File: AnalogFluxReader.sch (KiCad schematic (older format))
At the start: 54 parts, among them J1 , J2 , J3 , J4 , U1 AD9235BR, U2 74HC393, U3 AD8138, U4 74HC06, U5 74HC06, U6 LM2664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

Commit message: Updated schematic. Use 74AC163 and 74AC153 instead.
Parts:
- removed D1, D2, D3, D4, D5: BAT54HMFH, symbol Device:D
- removed JP1, JP2, JP3, JP4, JP5, JP6, JP7, JP8: Jumper, symbol Device:Jumper
- removed R3: 1k, symbol Device:R
- removed U2: 74HC393, symbol 74xx:74LS393
- removed unit 2 of U4
- removed unit 1 of U5
- added U2: 74AC163, symbol 74xx:74LS163
- added U8: 74AC153, symbol 74xx:74LS153
- C10, C11: value 100n -> 15p
- C12, C9: value CP_Small -> 47u
- R10, R9: value 1k -> 22
- U4: value 74HC06 -> 74HC14
- U5: value 74HC06 -> 74HC05
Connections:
- net labels added: CLKSEL0, CLKSEL1
- net labels removed: DSKCHG, REDWC
- wire segments 254 -> 255
- no-connect marks 13 -> 17

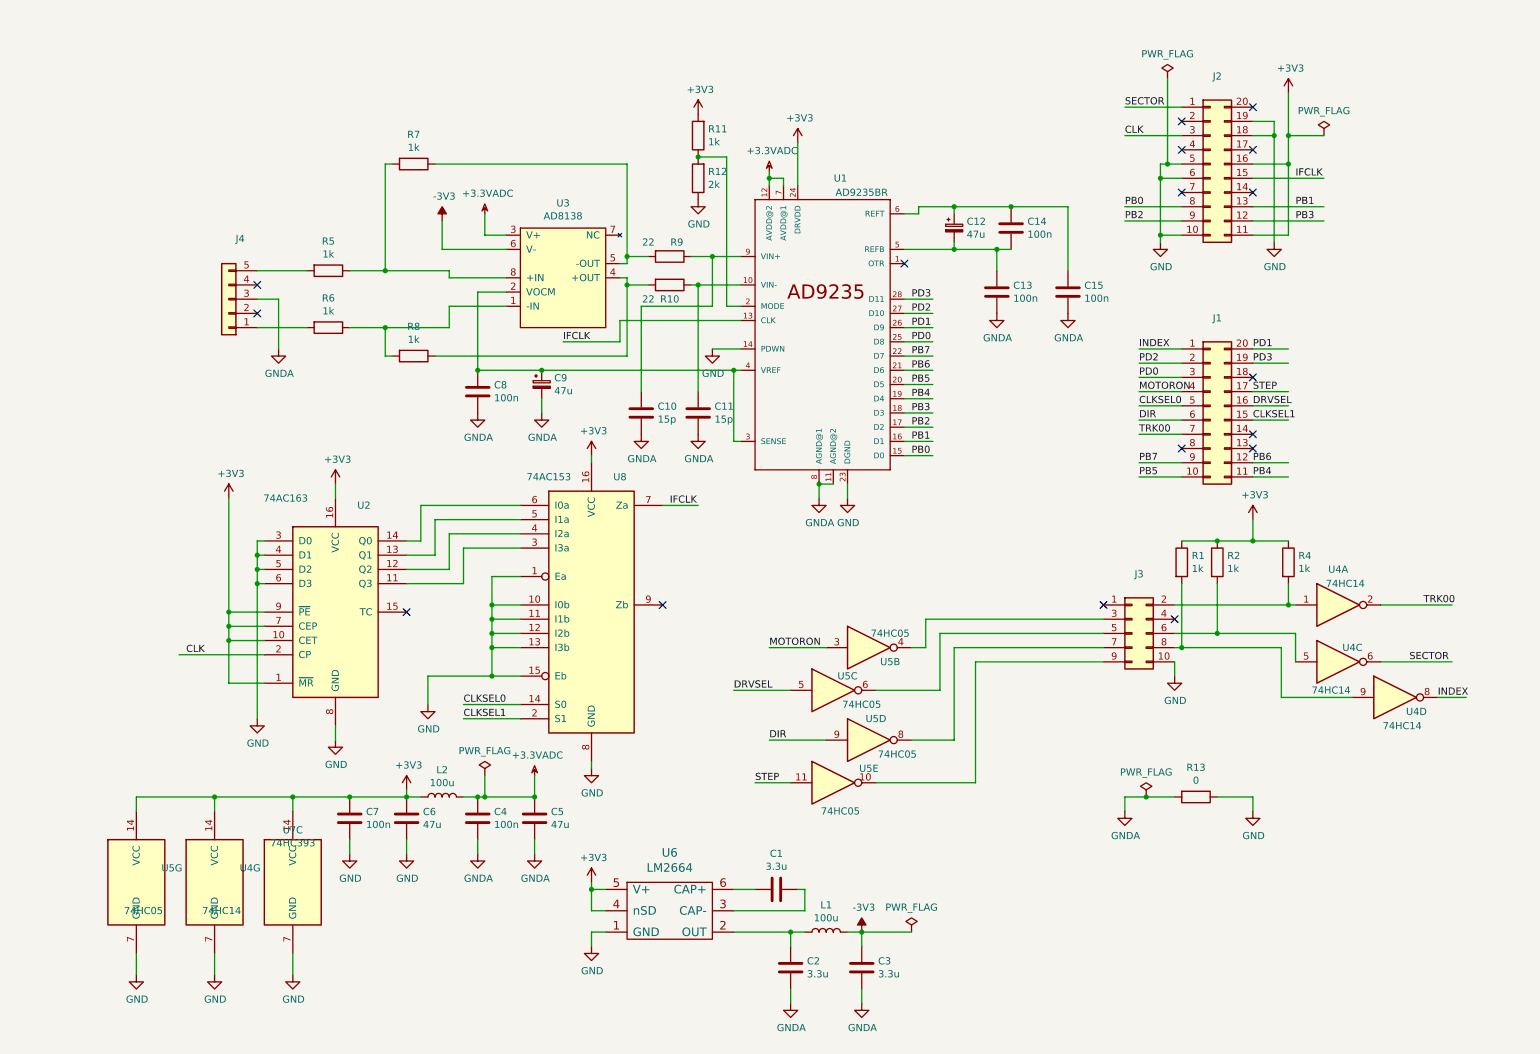
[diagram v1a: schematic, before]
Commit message: Introduced MCP23017 to handle low speed floppy signals. Several PAx pins needed for Slave FIFO.
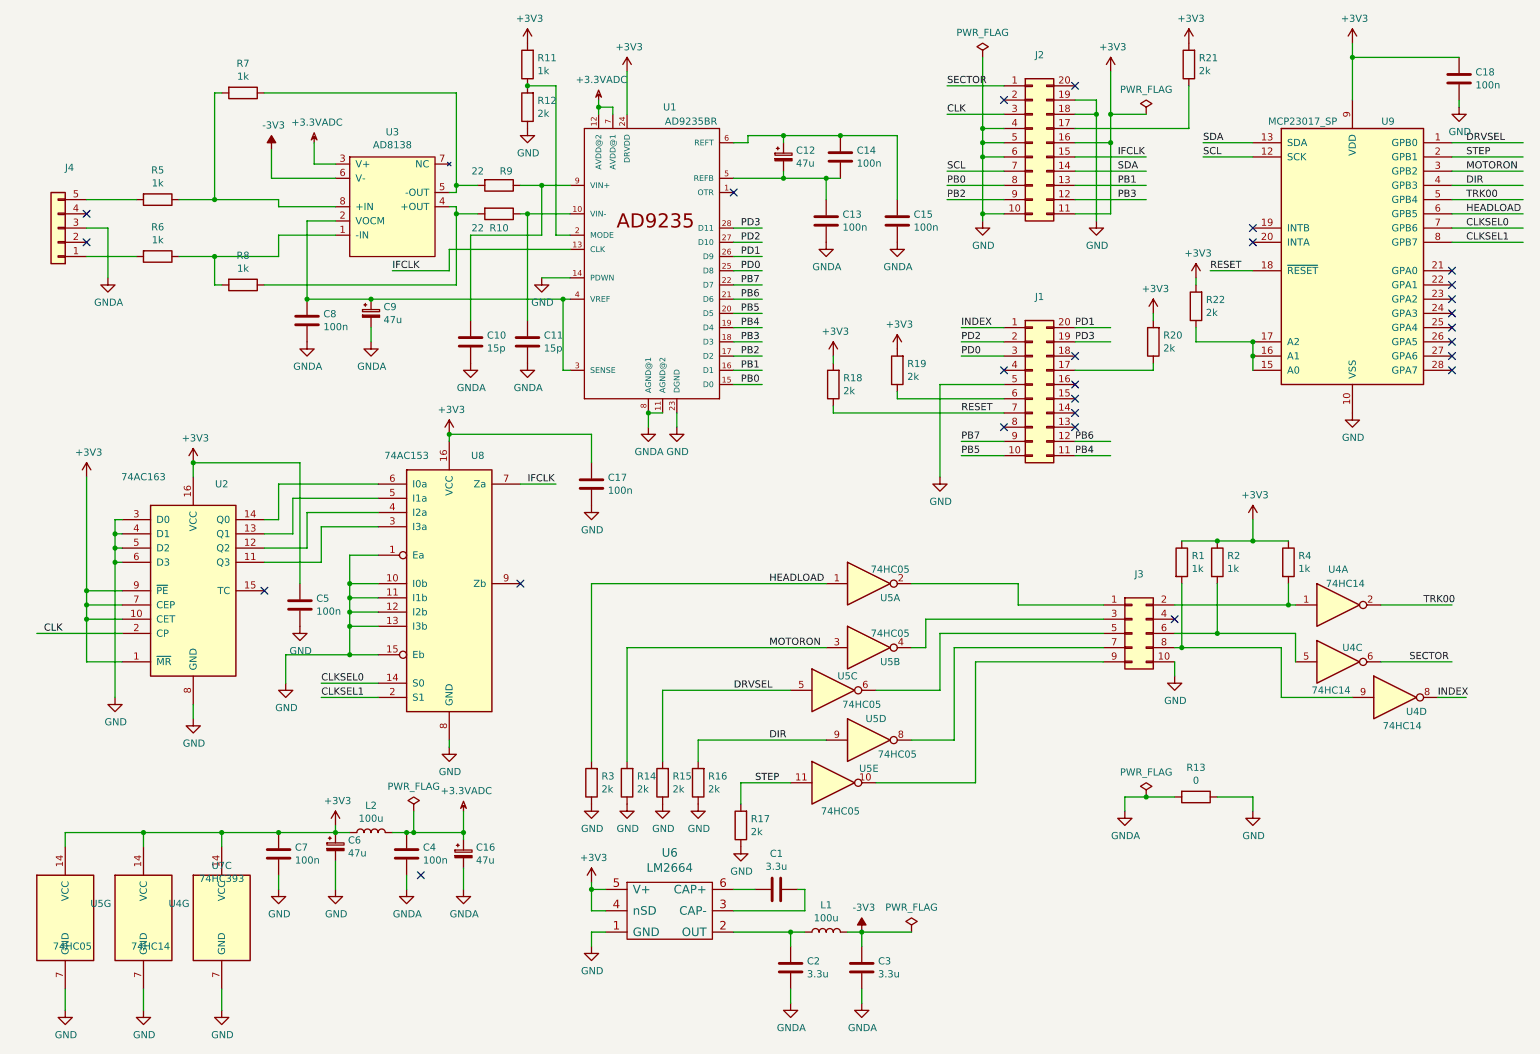
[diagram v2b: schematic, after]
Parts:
- removed C6: 47u, symbol Device:C
- added C16, C6: 47u, symbol Device:CP_Small
- added C17, C18: 100n, symbol Device:C
- added R14, R15, R16, R17, R18, R19, R20, R21, R22, R3: 2k, symbol Device:R
- added unit 1 of U5
- added U9: MCP23017_SP, Package_DIP:DIP-28_W7.62mm, symbol Interface_Expansion:MCP23017_SP
- C5: value 47u -> 100n
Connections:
- net labels added: HEADLOAD, RESET, SCL, SDA
- wire segments 255 -> 297
- no-connect marks 17 -> 26
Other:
- moved on the sheet: C10, C11, C12, C13, C14, C15, C4, C7, C8, C9, J1, J2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

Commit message: Added 1007 layout. Assigned footprints.
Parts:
- removed J1, J2: (no value), symbol Connector_Generic:Conn_02x10_Counter_Clockwise
- removed J4: (no value), symbol Connector_Generic:Conn_01x05
- removed U7: 74HC393, symbol 74xx:74LS393
- added J1, J2: Conn_02x10_Odd_Even, Connector_PinHeader_2.54mm:PinHeader_2x10_P2.54mm_Vertical, symbol Connector_Generic:Conn_02x10_Odd_Even
- added J4: FLOPPY+, Connector_PinHeader_2.54mm:PinHeader_1x01_P2.54mm_Vertical, symbol Connector:Conn_01x01_Male
- added J5: FLOPPY-GND, Connector_PinHeader_2.54mm:PinHeader_1x01_P2.54mm_Vertical, symbol Connector:Conn_01x01_Male
- added J6: FLOPPY-, Connector_PinHeader_2.54mm:PinHeader_1x01_P2.54mm_Vertical, symbol Connector:Conn_01x01_Male
- C1, C12, C16, C2, C3, C6, C9: footprint (none) -> Capacitor_SMD:CP_Elec_4x5.4
- C10, C11, C13, C14, C15, C17, C18, C4, C5, C7, C8: footprint (none) -> Capacitor_SMD:C_0805_2012Metric_Pad1.15x1.40mm_HandSolder
- J3: footprint (none) -> Connector_PinHeader_2.54mm:PinHeader_2x05_P2.54mm_Vertical
- L1, L2: footprint (none) -> AnalogFluxReader:1007
- R1, R10, R11, R12, R14, R15, R16, R17, R18, R19, R2, R20, R21, R22, R3, R4, R9: footprint (none) -> Resistor_SMD:R_0805_2012Metric_Pad1.15x1.40mm_HandSolder
- R13, R5, R6, R7, R8: footprint (none) -> Resistor_THT:R_Axial_DIN0207_L6.3mm_D2.5mm_P7.62mm_Horizontal
- U1: footprint (none) -> Package_SO:TSSOP-28_4.4x9.7mm_P0.65mm
- U2, U8: footprint (none) -> Package_SO:SOIC-16_3.9x9.9mm_P1.27mm
- U3: footprint agg:SOIC-8 -> Package_SO:SOIC-8_3.9x4.9mm_P1.27mm
- U4, U5: footprint (none) -> Package_SO:SOIC-14_3.9x8.7mm_P1.27mm
- U6: footprint (none) -> Package_TO_SOT_SMD:SOT-23-6_Handsoldering
- U9: footprint Package_DIP:DIP-28_W7.62mm -> Package_SO:SSOP-28_5.3x10.2mm_P0.65mm
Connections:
- wire segments 297 -> 294
- no-connect marks 26 -> 24

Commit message: Layout done. Some fixes to schematic.
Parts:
- removed J3: (no value), Connector_PinHeader_2.54mm:PinHeader_2x05_P2.54mm_Vertical, symbol Connector_Generic:Conn_02x05_Odd_Even
- added C19, C20, C21, C22: 100n, Capacitor_SMD:C_0805_2012Metric_Pad1.15x1.40mm_HandSolder, symbol Device:C
- added J3: Conn_02x05_Top_Bottom, symbol Connector_Generic:Conn_02x05_Top_Bottom
- added unit 4 of U4
- added unit 5 of U4
- added unit 6 of U4
- added unit 6 of U5
- renumbered J2 to J1, J1 to J2
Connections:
- wire segments 294 -> 326
- no-connect marks 24 -> 19
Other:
- moved on the sheet: C1, C16, C2, C3, C4, C6, C7, L1, L2, U6

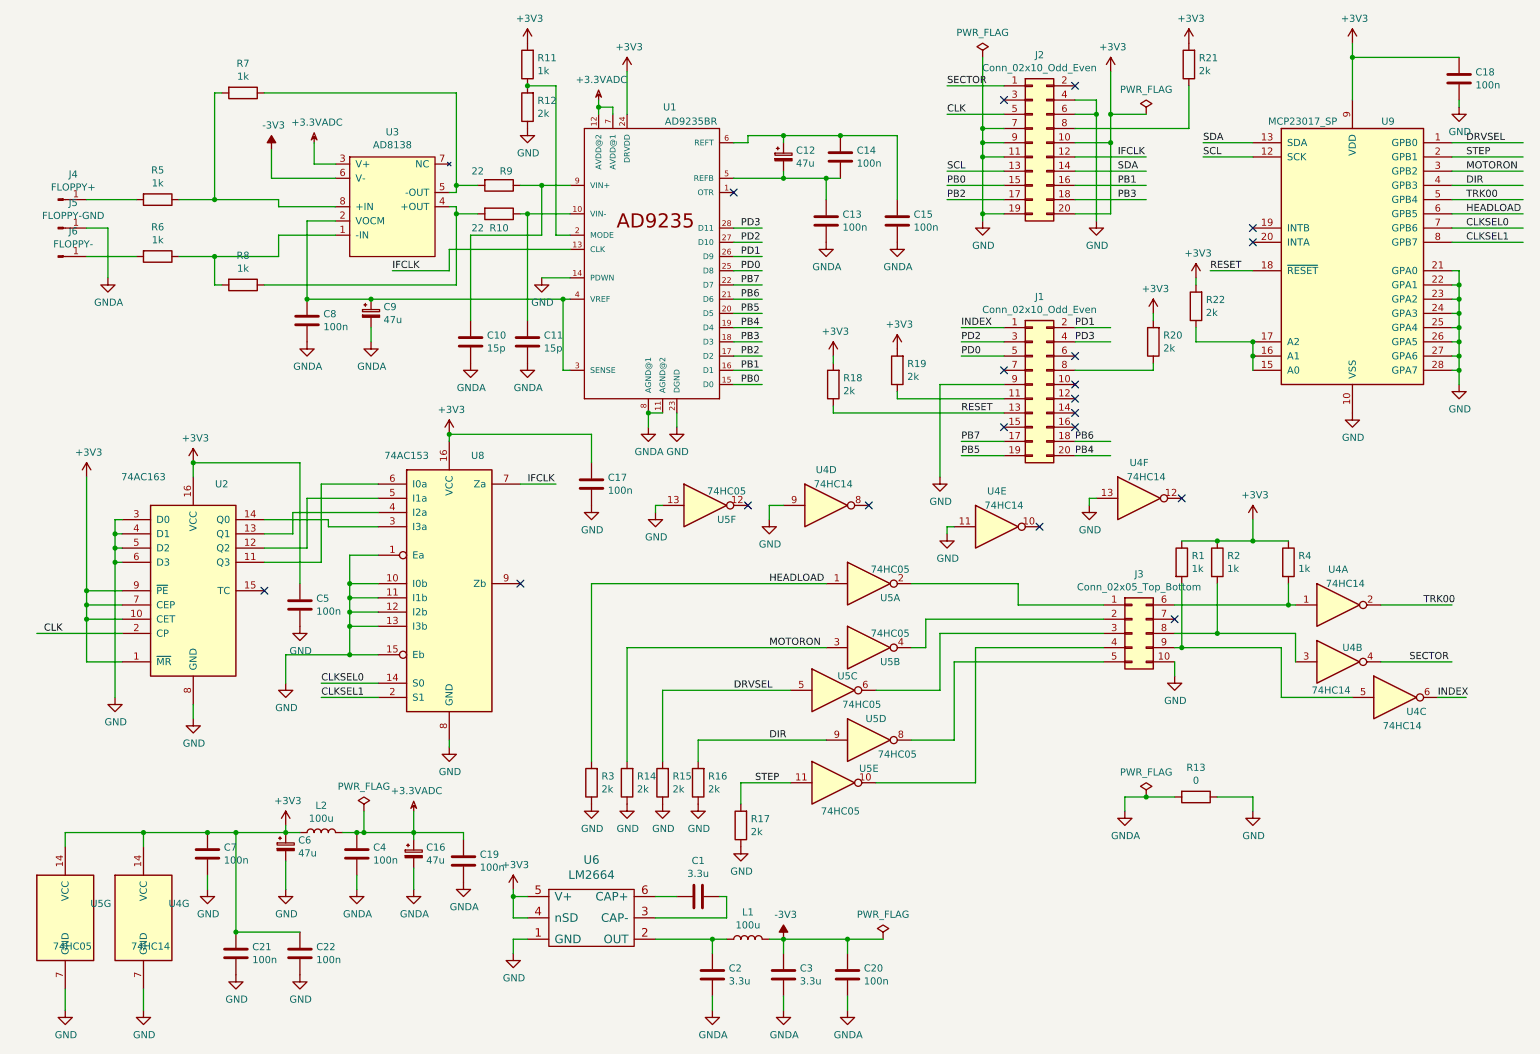
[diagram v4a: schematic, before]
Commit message: Review found some issues.
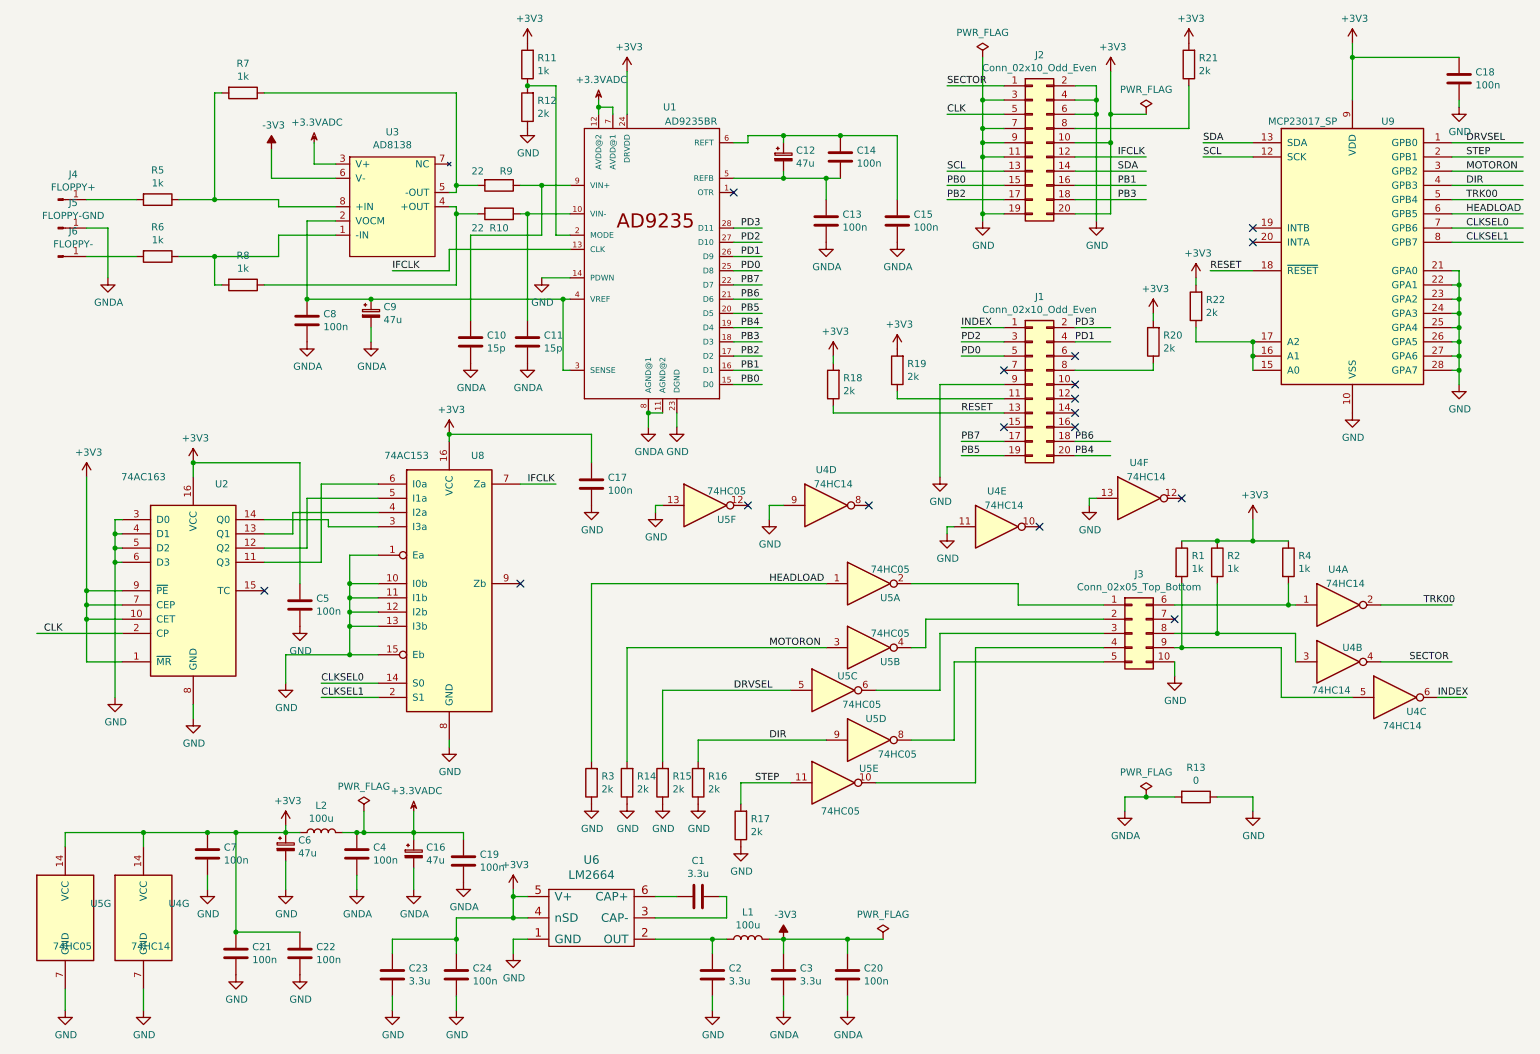
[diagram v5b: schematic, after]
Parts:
- added C23: 3.3u, Capacitor_SMD:CP_Elec_4x5.4, symbol Device:C
- added C24: 100n, Capacitor_SMD:C_0805_2012Metric_Pad1.15x1.40mm_HandSolder, symbol Device:C
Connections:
- wire segments 326 -> 337
- no-connect marks 19 -> 17
